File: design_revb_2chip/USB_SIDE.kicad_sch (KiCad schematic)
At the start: 53 parts, among them J1 USB_C_Receptacle, J2 Conn_01x08, U1 LAN7801-I/9JX, U2 TPS62162QDSGRQ1, U3 93C56A-I/P

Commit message: Preliminary Footprint Assignments
- initial footprint assignments
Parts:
- C1, C10, C11, C12, C13, C14, C15, C16, C17, C18, C19, C2, C20, C21, C22, C23, C24, C25, C26, C3, C4, C5, C6, C7, C8, C9: footprint (none) -> Capacitor_SMD:C_0201_0603Metric
- D1, D2: footprint (none) -> LED_SMD:LED_0603_1608Metric
- FB1, FB2: footprint (none) -> Capstone_Footprints:BEADC1608X95N
- L1: footprint (none) -> Inductor_SMD_Wurth:L_Wurth_WE-LQSH-3012
- L2: footprint (none) -> Inductor_SMD:L_1008_2520Metric
- R1, R10, R11, R12, R13, R14, R15, R2, R3, R4, R5, R6, R7, R8, R9: footprint (none) -> Resistor_SMD:R_0805_2012Metric
- U1: footprint SQFN64_9JX_MCH -> Capstone_Footprints:SQFN64_9JX_MCH
- U2: footprint DSG0008A -> Capstone_Footprints:DSG0008A
- U3: footprint PDIP8_300MC_MCH -> Capstone_Footprints:PDIP8_300MC_MCH
- XTAL1: footprint ECX-2236B2_ECS -> Capstone_Footprints:ECX-2236B2_ECS
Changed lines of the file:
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@@
 			)
 		)
-		(property "Footprint" ""
+		(property "Footprint" "Capacitor_SMD:C_0201_0603Metric"
 			(at 53.0352 243.84 0)
 			(effects
@@
 			)
 		)
-		(property "Footprint" ""
+		(property "Footprint" "Inductor_SMD_Wurth:L_Wurth_WE-LQSH-3012"
 			(at 111.76 194.31 0)
 			(effects
@@
 			)
 		)
-		(property "Footprint" ""
+		(property "Footprint" "Resistor_SMD:R_0805_2012Metric"
 			(at 204.724 143.256 90)
 			(effects
@@
 			)
 		)
-		(property "Footprint" ""
+		(property "Footprint" "Capacitor_SMD:C_0201_0603Metric"
 			(at 61.9252 87.63 0)
 			(effects
@@
 			)
 		)
-		(property "Footprint" ""
+		(property "Footprint" "Capacitor_SMD:C_0201_0603Metric"
 			(at 65.7352 243.84 0)
 			(effects
@@
 			)
 		)
-		(property "Footprint" ""
+		(property "Footprint" "LED_SMD:LED_0603_1608Metric"
 			(at 182.88 147.32 0)
 			(effects
@@
 			)
 		)
-		(property "Footprint" "ECX-2236B2_ECS"
+		(property "Footprint" "Capstone_Footprints:ECX-2236B2_ECS"
 			(at 321.564 124.714 0)
 			(effects
@@
 			)
 		)
-		(property "Footprint" ""
+		(property "Footprint" "Resistor_SMD:R_0805_2012Metric"
 			(at 239.014 190.246 90)
 			(effects
@@
 			)
 		)
-		(property "Footprint" ""
+		(property "Footprint" "Capacitor_SMD:C_0201_0603Metric"
 			(at 55.5752 195.58 0)
 			(effects
@@
 			)
 		)
-		(property "Footprint" ""
+		(property "Footprint" "Capacitor_SMD:C_0201_0603Metric"
 			(at 105.1052 203.2 0)
 			(effects
@@
 			)
 		)
-		(property "Footprint" ""
+		(property "Footprint" "Resistor_SMD:R_0805_2012Metric"
 			(at 213.614 202.946 90)
 			(effects
@@
 			)
 		)
-		(property "Footprint" "DSG0008A"
+		(property "Footprint" "Capstone_Footprints:DSG0008A"
 			(at 198.12 245.11 0)
 			(effects
@@
 			)
 		)
-		(property "Footprint" ""
+		(property "Footprint" "Capacitor_SMD:C_0201_0603Metric"
 			(at 89.8652 195.58 0)
 			(effects
@@
 			)
 		)
-		(property "Footprint" ""
+		(property "Footprint" "Resistor_SMD:R_0805_2012Metric"
 			(at 212.344 169.926 90)
 			(effects
@@
 			)
 		)
-		(property "Footprint" ""
+		(property "Footprint" "Resistor_SMD:R_0805_2012Metric"
 			(at 305.054 190.246 90)
 			(effects
@@
 			)
 		)
-		(property "Footprint" ""
+		(property "Footprint" "Capacitor_SMD:C_0201_0603Metric"
 			(at 256.2352 248.92 0)
 			(effects
@@
 			)
 		)
-		(property "Footprint" ""
+		(property "Footprint" "Capacitor_SMD:C_0201_0603Metric"
 			(at 106.3752 243.84 0)
 			(effects
@@
 			)
 		)
-		(property "Footprint" ""
+		(property "Footprint" "Capacitor_SMD:C_0201_0603Metric"
 			(at 78.4352 243.84 0)
 			(effects
@@
 			)
 		)
-		(property "Footprint" ""
+		(property "Footprint" "Capstone_Footprints:BEADC1608X95N"
 			(at 147.828 223.52 90)
 			(effects
@@
 			)
 		)
-		(property "Footprint" ""
+		(property "Footprint" "Resistor_SMD:R_0805_2012Metric"
 			(at 160.274 235.966 90)
 			(effects
@@
 			)
 		)
-		(property "Footprint" "PDIP8_300MC_MCH"
+		(property "Footprint" "Capstone_Footprints:PDIP8_300MC_MCH"
 			(at 228.092 116.078 0)
 			(effects
@@
 			)
 		)
-		(property "Footprint" ""
+		(property "Footprint" "Capacitor_SMD:C_0201_0603Metric"
 			(at 268.9352 140.97 0)
 			(effects
@@
 			)
 		)
-		(property "Footprint" ""
+		(property "Footprint" "Capacitor_SMD:C_0201_0603Metric"
 			(at 219.4052 86.36 0)
 			(effects
@@
 			)
 		)
-		(property "Footprint" ""
+		(property "Footprint" "Resistor_SMD:R_0805_2012Metric"
 			(at 192.786 148.336 90)
 			(effects
@@
 			)
 		)
-		(property "Footprint" ""
+		(property "Footprint" "Capacitor_SMD:C_0201_0603Metric"
 			(at 318.4652 143.51 0)
 			(effects
@@
 			)
 		)
-		(property "Footprint" ""
+		(property "Footprint" "Resistor_SMD:R_0805_2012Metric"
 			(at 235.204 237.236 90)
 			(effects
@@
 			)
 		)
-		(property "Footprint" ""
+		(property "Footprint" "Capacitor_SMD:C_0201_0603Metric"
 			(at 187.6552 191.77 0)
 			(effects
@@
 			)
 		)
-		(property "Footprint" ""
+		(property "Footprint" "Resistor_SMD:R_0805_2012Metric"
 			(at 254.254 140.716 90)
 			(effects
@@
 			)
 		)
-		(property "Footprint" ""
+		(property "Footprint" "Capacitor_SMD:C_0201_0603Metric"
 			(at 318.4652 194.31 0)
 			(effects
@@
 			)
 		)
-		(property "Footprint" ""
+		(property "Footprint" "Capacitor_SMD:C_0201_0603Metric"
 			(at 120.3452 243.84 0)
 			(effects
@@
 			)
 		)
-		(property "Footprint" ""
+		(property "Footprint" "Capacitor_SMD:C_0201_0603Metric"
 			(at 44.1452 195.58 0)
 			(effects
@@
 			)
 		)
-		(property "Footprint" ""
+		(property "Footprint" "Capstone_Footprints:BEADC1608X95N"
 			(at 96.52 188.468 90)
 			(effects
@@
 			)
 		)
-		(property "Footprint" ""
+		(property "Footprint" "Capacitor_SMD:C_0201_0603Metric"
 			(at 40.3352 243.84 0)
 			(effects
@@
 			)
 		)
-		(property "Footprint" ""
+		(property "Footprint" "Capacitor_SMD:C_0201_0603Metric"
 			(at 162.2552 248.92 0)
 			(effects
@@
 			)
 		)
-		(property "Footprint" ""
+		(property "Footprint" "Resistor_SMD:R_0805_2012Metric"
 			(at 227.584 78.486 90)
 			(effects
@@
 			)
 		)
-		(property "Footprint" ""
+		(property "Footprint" "Capacitor_SMD:C_0201_0603Metric"
 			(at 67.0052 195.58 0)
 			(effects
@@
 			)
 		)
-		(property "Footprint" ""
+		(property "Footprint" "Capacitor_SMD:C_0201_0603Metric"
 			(at 354.0252 148.59 0)
 			(effects
@@
 			)
 		)
-		(property "Footprint" ""
+		(property "Footprint" "Capacitor_SMD:C_0201_0603Metric"
 			(at 51.7652 83.82 0)
 			(effects
@@
 			)
 		)
-		(property "Footprint" ""
+		(property "Footprint" "Capacitor_SMD:C_0201_0603Metric"
 			(at 78.4352 195.58 0)
 			(effects
@@
 			)
 		)
-		(property "Footprint" "SQFN64_9JX_MCH"
+		(property "Footprint" "Capstone_Footprints:SQFN64_9JX_MCH"
 			(at 165.1 73.66 0)
 			(effects
@@
 			)
 		)
-		(property "Footprint" ""
+		(property "Footprint" "Resistor_SMD:R_0805_2012Metric"
 			(at 186.436 120.396 90)
 			(effects
@@
 			)
 		)
-		(property "Footprint" ""
+		(property "Footprint" "Capacitor_SMD:C_0201_0603Metric"
 			(at 265.1252 180.34 0)
 			(effects
@@
 			)
 		)
-		(property "Footprint" ""
+		(property "Footprint" "Inductor_SMD:L_1008_2520Metric"
 			(at 226.06 232.41 0)
 			(effects
@@
 			)
 		)
-		(property "Footprint" ""
+		(property "Footprint" "Resistor_SMD:R_0805_2012Metric"
 			(at 265.684 253.746 90)
 			(effects
@@
 			)
 		)
-		(property "Footprint" ""
+		(property "Footprint" "Resistor_SMD:R_0805_2012Metric"
 			(at 244.094 253.746 90)
 			(effects
@@
 			)
 		)
-		(property "Footprint" ""
+		(property "Footprint" "LED_SMD:LED_0603_1608Metric"
 			(at 266.7 237.49 0)
 			(effects
@@
 			)
 		)
-		(property "Footprint" ""
+		(property "Footprint" "Capacitor_SMD:C_0201_0603Metric"
 			(at 174.9552 191.77 0)
 			(effects
@@
 			)
 		)
-		(property "Footprint" ""
+		(property "Footprint" "Resistor_SMD:R_0805_2012Metric"
 			(at 244.094 237.236 90)
 			(effects
@@
 			)
 		)
-		(property "Footprint" ""
+		(property "Footprint" "Resistor_SMD:R_0805_2012Metric"
 			(at 65.024 93.726 90)
 			(effects
@@
 			)
 		)
-		(property "Footprint" ""
+		(property "Footprint" "Capacitor_SMD:C_0201_0603Metric"
 			(at 92.4052 243.84 0)
 			(effects
@@
 			)
 		)
-		(property "Footprint" ""
+		(property "Footprint" "Capacitor_SMD:C_0201_0603Metric"
 			(at 147.0152 245.11 0)
 			(effects

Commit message: PCB Created
Footprints all placed in the PCB document
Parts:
- J2: footprint (none) -> Connector_PinHeader_2.00mm:PinHeader_1x08_P2.00mm_Horizontal
- R6, R8: footprint Resistor_SMD:R_0805_2012Metric -> Resistor_SMD:R_0402_1005Metric
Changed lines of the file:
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@@
 			)
 		)
-		(property "Footprint" ""
+		(property "Footprint" "Connector_PinHeader_2.00mm:PinHeader_1x08_P2.00mm_Horizontal"
 			(at 251.46 53.34 0)
 			(effects
@@
 			)
 		)
-		(property "Footprint" "Resistor_SMD:R_0805_2012Metric"
+		(property "Footprint" "Resistor_SMD:R_0402_1005Metric"
 			(at 212.344 169.926 90)
 			(effects
@@
 			)
 		)
-		(property "Footprint" "Resistor_SMD:R_0805_2012Metric"
+		(property "Footprint" "Resistor_SMD:R_0402_1005Metric"
 			(at 227.584 78.486 90)
 			(effects

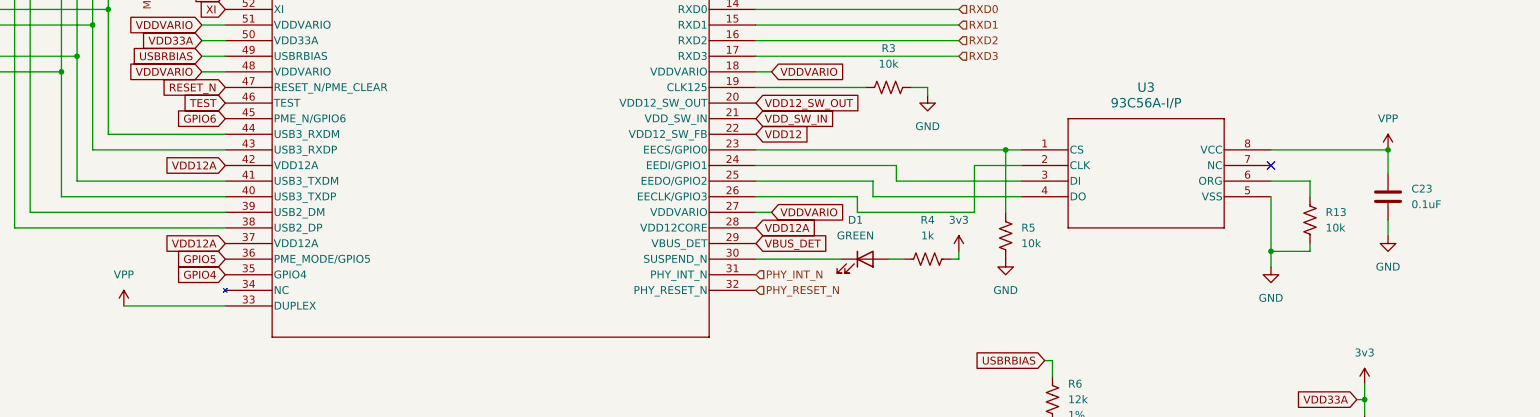
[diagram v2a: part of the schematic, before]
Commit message: Some PCB Design
- USB side PCB design (mostly done)
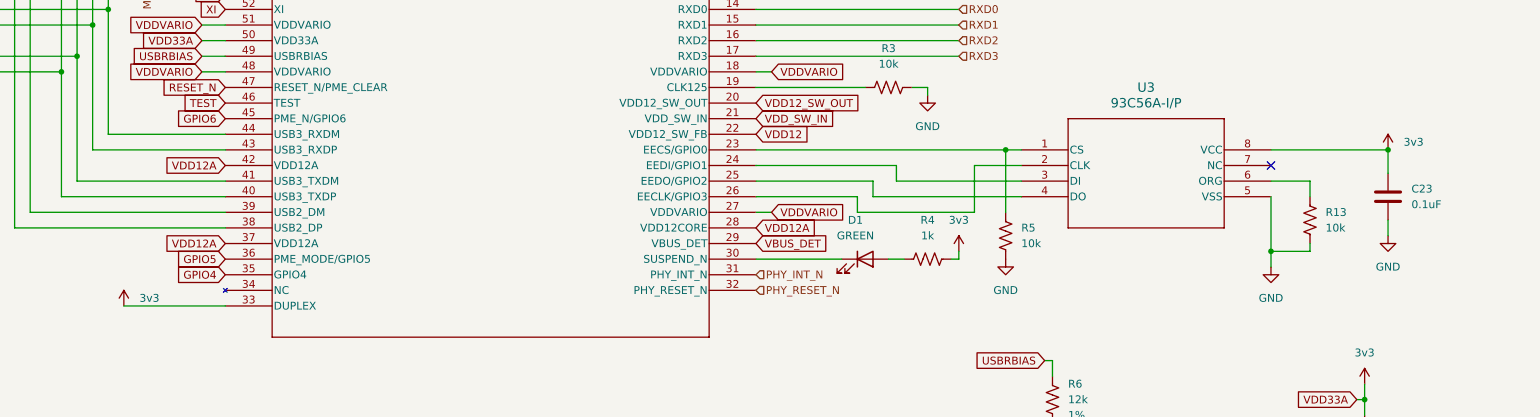
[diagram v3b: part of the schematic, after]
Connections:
- net VPP is gone; now on net 3v3: C23.1, U1.33 (DUPLEX), U3.8 (VCC)
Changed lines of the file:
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@@
 			)
 		)
-		(property "Value" "VPP"
-			(at 62.23 149.86 0)
-			(effects
-				(font
-					(size 1.27 1.27)
-				)
+		(property "Value" "3v3"
+			(at 64.77 153.6699 0)
+			(effects
+				(font
+					(size 1.27 1.27)
+				)
+				(justify left)
 			)
 		)
@@
 			)
 		)
-		(property "Value" "VPP"
-			(at 267.97 124.46 0)
-			(effects
-				(font
-					(size 1.27 1.27)
-				)
-			)
-		)
+		(property "Value" "3v3"
+			(at 270.51 128.2699 0)
+			(effects
+				(font
+					(size 1.27 1.27)
+				)
+				(justify left)
+			)
+		)
